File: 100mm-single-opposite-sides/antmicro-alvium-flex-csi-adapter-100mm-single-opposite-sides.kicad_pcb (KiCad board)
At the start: 2 copper layers, 25.5 x 100.1 mm, 3 parts, among them J1 WE_687622100002_FLEX, J2 WE_687650100002_FLEX

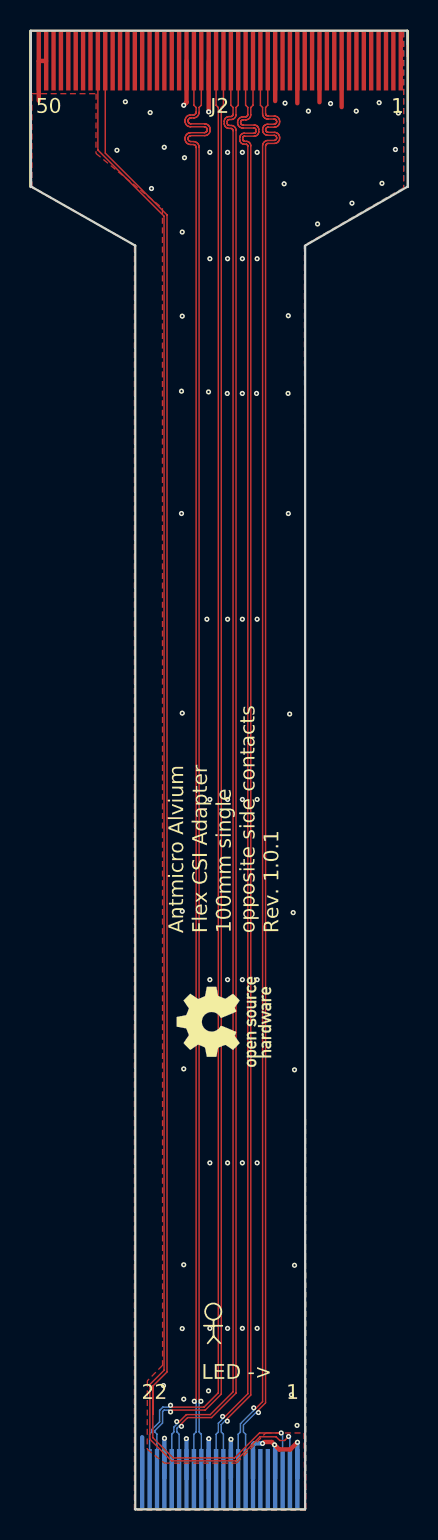
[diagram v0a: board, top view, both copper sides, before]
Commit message: Update naming convention
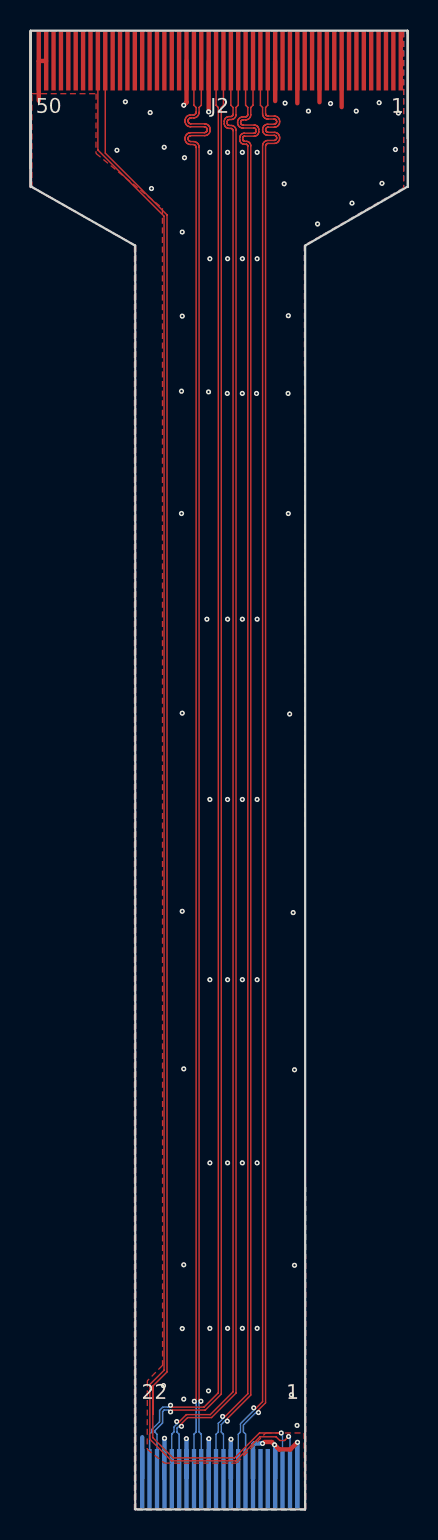
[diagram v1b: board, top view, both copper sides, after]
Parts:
- N1: moved to B.Cu
- moved N1 26.4 mm to (189.5, 105.3), turned to 270 degrees
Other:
- board text added: "<- LED"
- board text removed: "LED ->"

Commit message: 100mm-single-same: add NMOS transistor for camera triggering
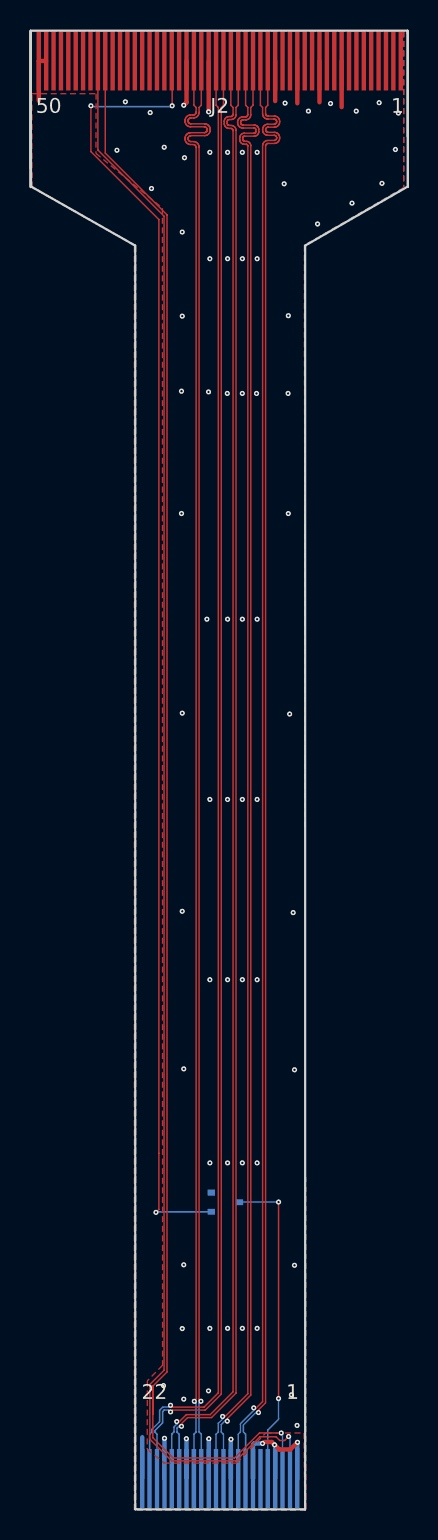
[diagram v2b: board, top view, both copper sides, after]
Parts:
- added Q1: BSS138APW, antmicro-alvium-flex-csi-adapter-footprints:SC70-3, B.Cu at (189.1, 144.0)
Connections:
- J2 pad 32: Net-(J2-Pad32) -> /VSYNC
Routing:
- net /VSYNC: track 0.00 -> 89.2 mm, vias 0 -> 3
- net /GPIO2: track 0.00 -> 21.7 mm, vias 0 -> 2
